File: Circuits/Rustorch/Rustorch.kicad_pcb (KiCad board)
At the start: 2 copper layers, 95 x 72 mm, 57 parts, among them CN1 USB_C_Receptacle_USB2.0_16P, CN2 OLED_128x64_IIC, Q1 2SC1815, Q2 2SC1815, Q3 2SC1815, Q4 2SC1815, SW1 SW_POWER (5P), SW2 RESET, SW3 SW_BOOT, SW4 SW_UP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

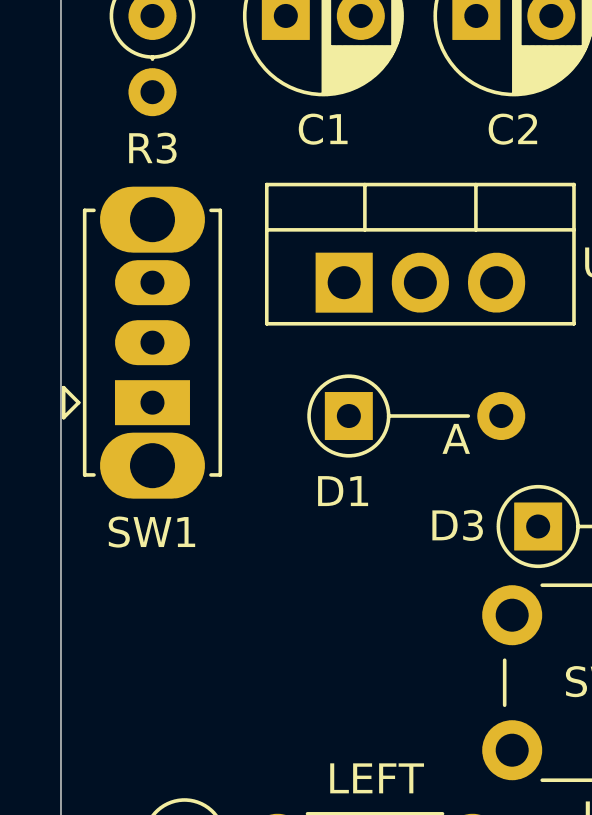
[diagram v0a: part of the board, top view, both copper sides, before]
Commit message: (Rustorch) 基板の電源スイッチを修正
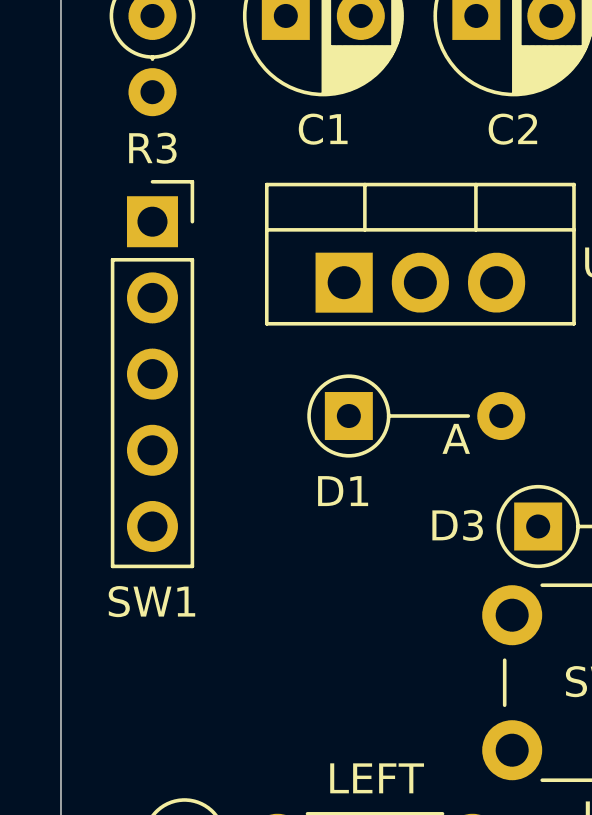
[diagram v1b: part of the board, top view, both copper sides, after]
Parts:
- SW1: value SW_POWER (5P) -> ToggleSW 3P; footprint Button_Switch_THT:SW_Slide_SPDT_Straight_CK_OS102011MS2Q -> Connector_PinSocket_2.54mm:PinSocket_1x05_P2.54mm_Vertical
- moved SW1 6.03 mm to (103.5, 97.0), turned to 0 degrees
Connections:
- SW1 pad 1: VBUS -> unconnected-(SW1-Pin_1-Pad1)
- SW1 pad 2: +5V -> unconnected-(SW1-Pin_2-Pad2)
- SW1 pad 3: unconnected-(SW1-C-Pad3) -> VBUS

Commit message: (Rustorch) 配線作業 (4層化)
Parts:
- moved R6 8.15 mm to (167.1, 109.7), turned to -90 degrees
- moved R1 7.62 mm to (113.5, 71.1), turned to -90 degrees
- moved R2 7.62 mm to (116.5, 71.1), turned to -90 degrees
- moved R5 3.05 mm to (164.0, 109.7)
- moved D2 2.55 mm to (103.5, 83.1), turned to -90 degrees
- moved C2 2.54 mm to (116.9, 90.1), turned to 180 degrees
- moved C3 2.50 mm to (116.9, 85.7), turned to 180 degrees
- moved R7 0.63 mm to (184.2, 97.1)
- turned BZ1 to 180 degrees
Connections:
- U3 pad 8: Net-(Q1-C) -> unconnected-(U3-CC-Pad8)
- U4 pad 8: Net-(Q2-C) -> unconnected-(U4-CC-Pad8)
- U5 pad 8: Net-(Q3-C) -> unconnected-(U5-CC-Pad8)
- U6 pad 8: Net-(Q4-C) -> unconnected-(U6-CC-Pad8)
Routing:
- net +3.3V: track 0.00 -> 111.0 mm, vias 0 -> 1
- net Net-(R11-Pad1): track 0.00 -> 89.9 mm
- net KEY_IN3_IO8: track 0.00 -> 78.3 mm
- net Net-(R10-Pad1): track 0.00 -> 77.3 mm
- net KEY_IN1_IO9_BOOT: track 0.00 -> 75.7 mm
- net /E: track 0.00 -> 72.4 mm, vias 0 -> 4
- net /DP: track 0.00 -> 67.5 mm, vias 0 -> 4
- net /D: track 0.00 -> 61.9 mm, vias 0 -> 4
- net /F: track 0.00 -> 60.2 mm, vias 0 -> 4
- net /C: track 0.00 -> 58.3 mm, vias 0 -> 4
- net 7SEG_DIGIT4: track 0.00 -> 57.8 mm
- net /G: track 0.00 -> 55.0 mm, vias 0 -> 4
- net /B: track 0.00 -> 53.3 mm, vias 0 -> 4
- net /A: track 0.00 -> 50.8 mm, vias 0 -> 4
- net 7SEG_DIGIT3: track 0.00 -> 44.0 mm
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- added copper zone on In1.Cu, net GND
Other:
- copper layers 2 -> 4

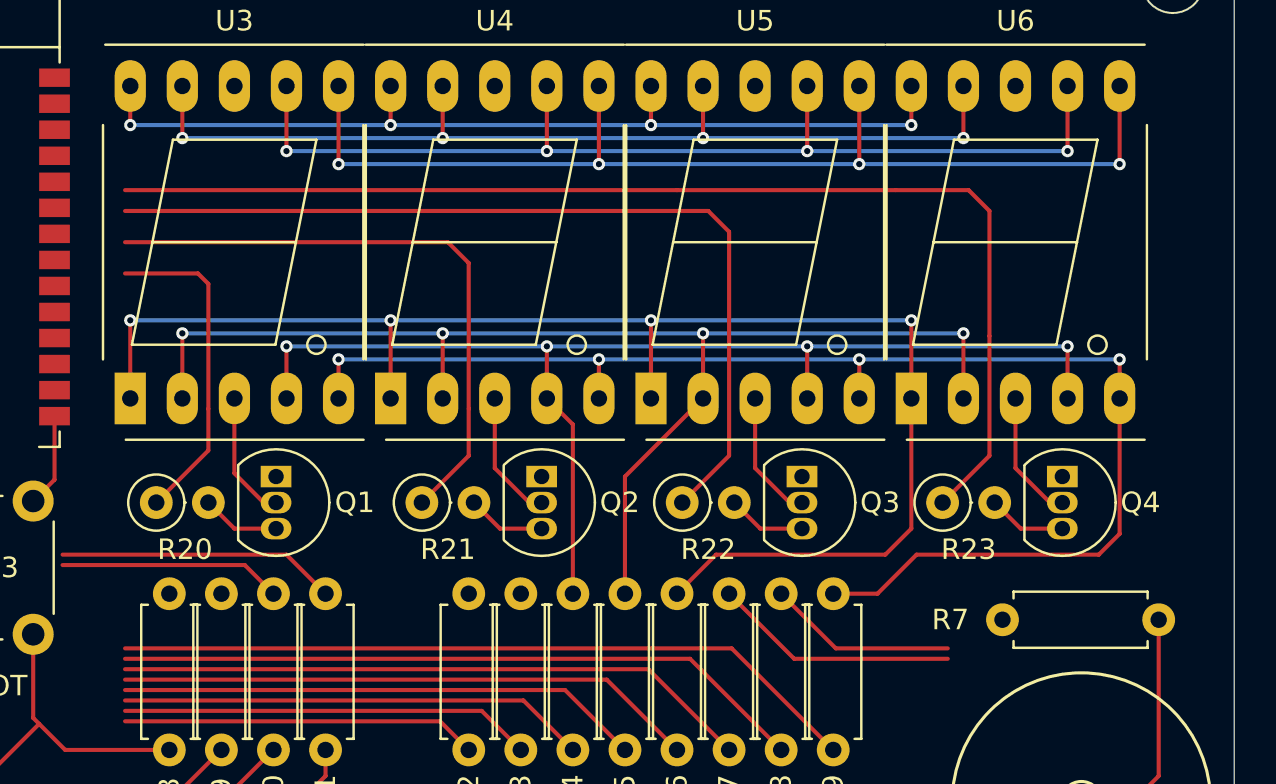
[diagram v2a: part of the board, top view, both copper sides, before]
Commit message: (Rustorch) 配線作業 (7セグ周辺)
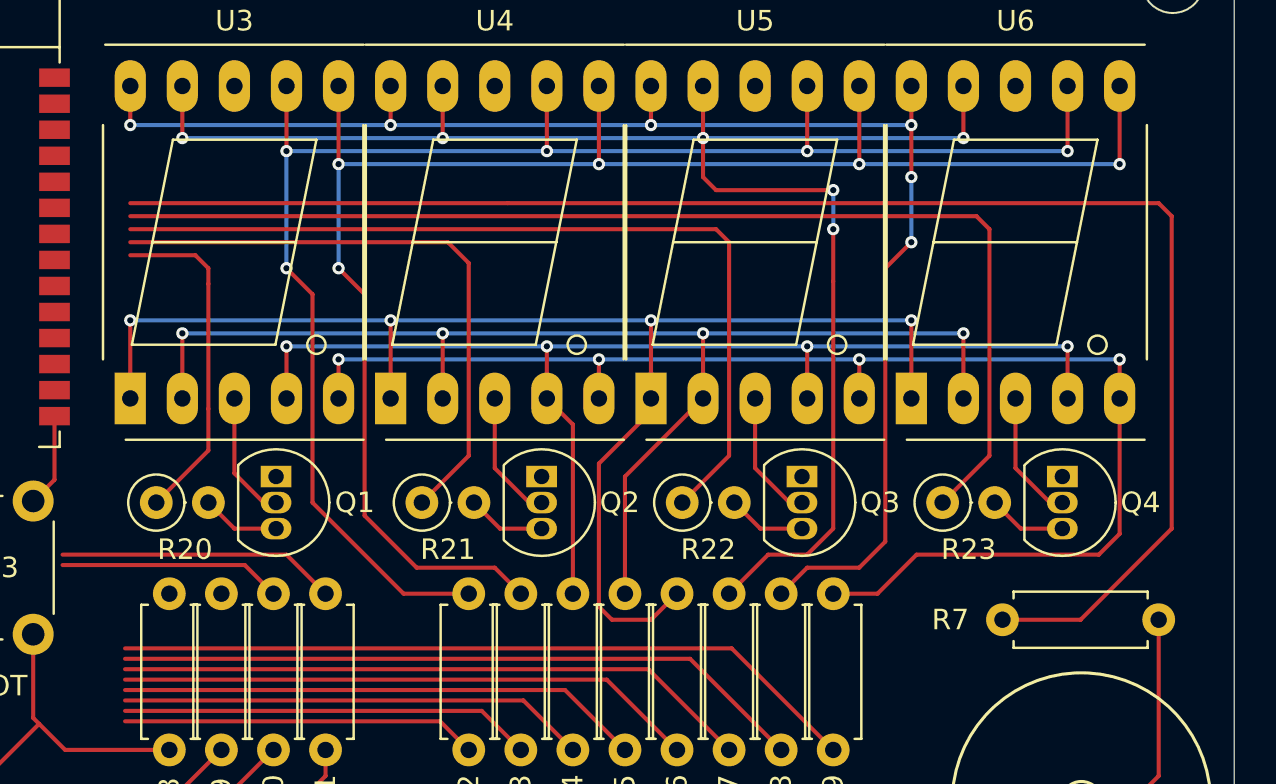
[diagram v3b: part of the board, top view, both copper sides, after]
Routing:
- net Net-(U1-MTMS/GPIO4/ADC1_CH4): track 0.00 -> 76.4 mm
- net /A: track 50.8 -> 77.9 mm, vias 4 -> 5
- net /B: track 53.3 -> 80.2 mm, vias 4 -> 5
- net /F: track 60.2 -> 79.7 mm, vias 4 -> 6
- net /G: track 55.0 -> 72.7 mm, vias 4 -> 6
- net Net-(D6-K): track 11.9 -> 18.4 mm
- net /E: track 72.4 -> 69.2 mm
- net 7SEG_DIGIT4: track 57.8 -> 56.5 mm
- net 7SEG_DIGIT3: track 44.0 -> 43.1 mm
- net 7SEG_DIGIT1: track 16.0 -> 16.6 mm

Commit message: (Rustorch) 配線作業 (一通り接続完了した状態)
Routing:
- net SDA: track 13.6 -> 74.8 mm, vias 0 -> 1
- net SCL: track 19.8 -> 77.9 mm, vias 0 -> 1
- net Net-(U1-MTDI/GPIO5/ADC1_CH5): track 25.5 -> 82.1 mm, vias 0 -> 3
- net KEY_IN2: track 20.3 -> 67.3 mm
- net KEY_IN3_IO8: track 78.3 -> 122.5 mm
- net 7SEG_E: track 28.3 -> 69.7 mm, vias 0 -> 2
- net 7SEG_D: track 25.6 -> 66.7 mm, vias 0 -> 2
- net 7SEG_A: track 17.5 -> 57.8 mm, vias 0 -> 2
- net 7SEG_B: track 20.1 -> 60.4 mm, vias 0 -> 2
- net 7SEG_C: track 22.8 -> 62.8 mm, vias 0 -> 2
- net KEY_OUT2: track 13.6 -> 50.0 mm, vias 0 -> 1
- net KEY_OUT1: track 10.9 -> 46.2 mm, vias 0 -> 1
- net 7SEG_G: track 33.8 -> 68.5 mm, vias 0 -> 2
- net 7SEG_DP: track 36.6 -> 70.9 mm
- net 7SEG_F: track 31.1 -> 65.3 mm, vias 0 -> 2
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- added copper zone on B.Cu, net GND
- added copper zone on F.Cu, net GND

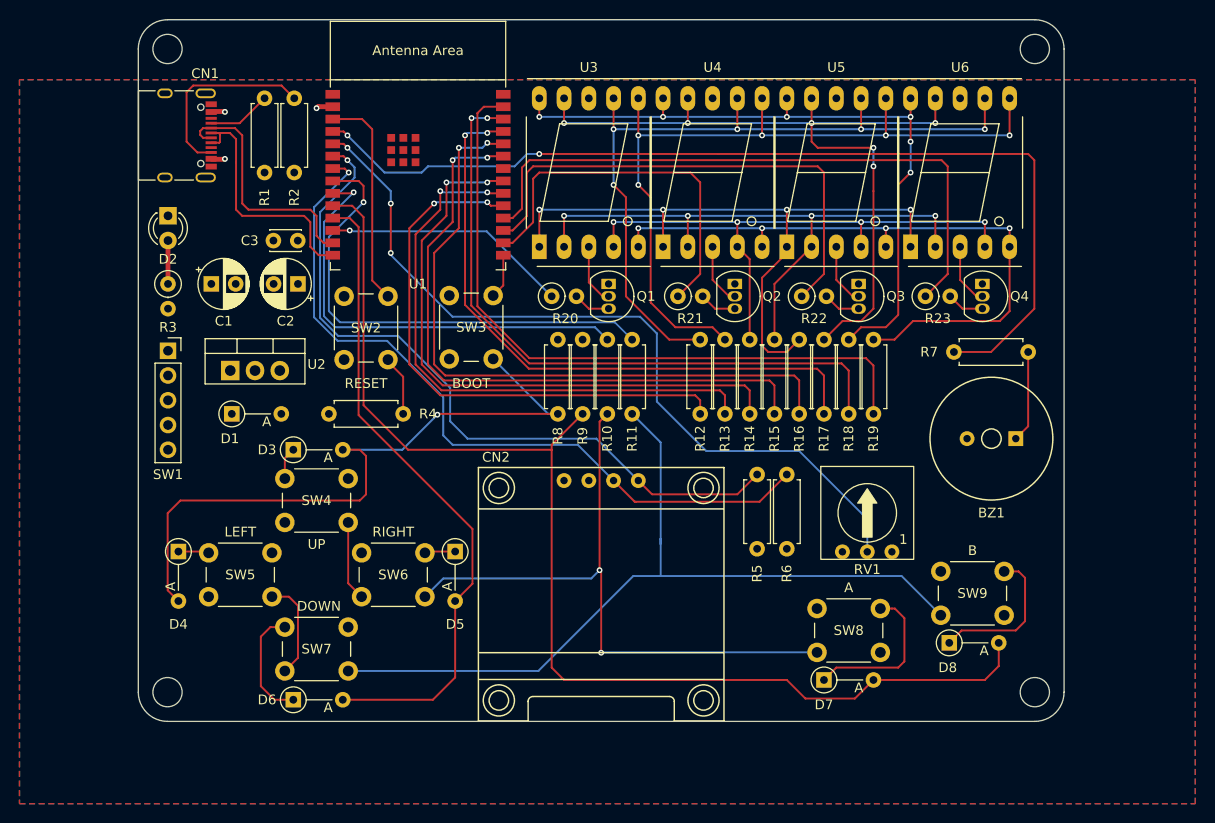
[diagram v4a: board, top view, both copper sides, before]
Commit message: (Rustorch) 配線作業 (表面に配線を集約中)
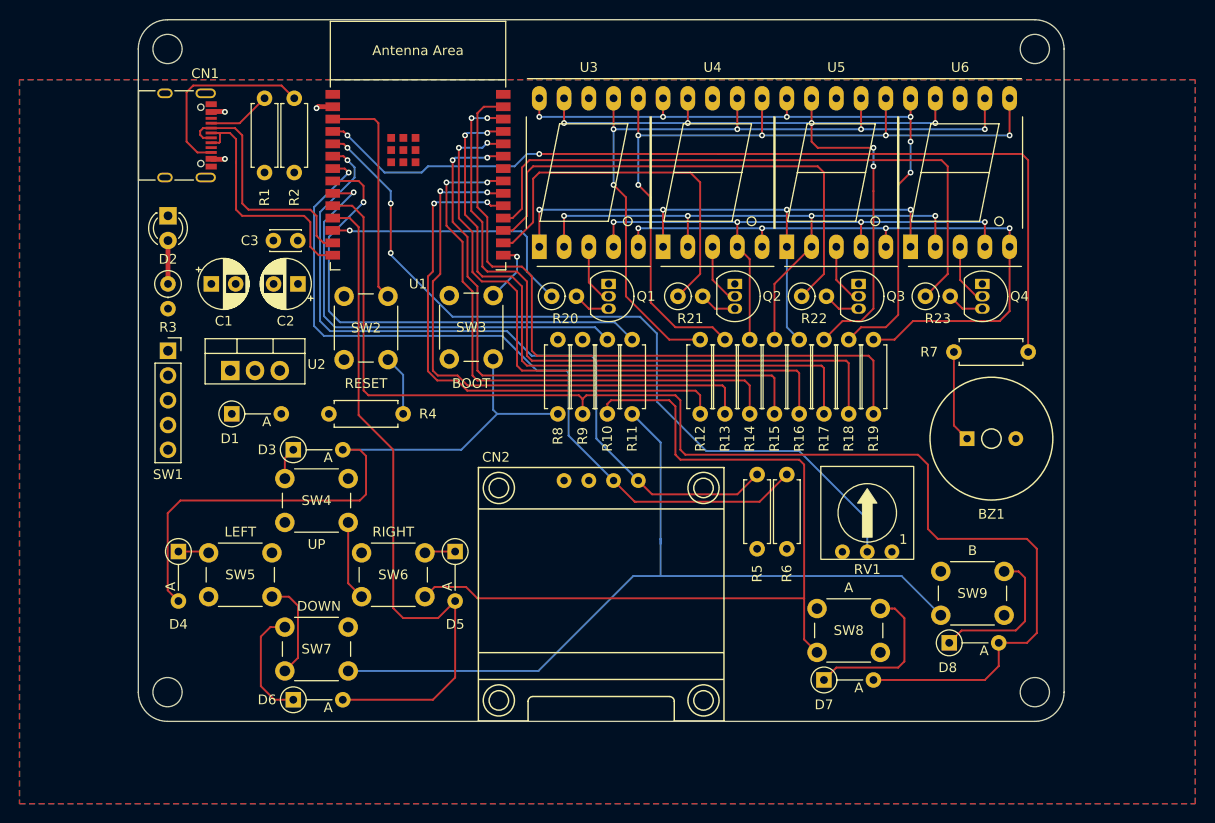
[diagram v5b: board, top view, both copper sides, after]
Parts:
- moved R7 7.62 mm to (191.8, 97.1), turned to 180 degrees
- turned BZ1 to 0 degrees
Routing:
- net Net-(R10-Pad1): track 93.8 -> 114.3 mm, vias 2 -> 0
- net KEY_IN3_IO8: track 122.5 -> 134.7 mm
- net Net-(U1-MTMS/GPIO4/ADC1_CH4): track 100.1 -> 93.8 mm
- net /E: track 69.2 -> 63.4 mm
- net 7SEG_E: track 69.7 -> 64.6 mm
- net 7SEG_D: track 66.7 -> 62.5 mm
- net 7SEG_C: track 62.8 -> 58.6 mm
- net KEY_IN2: track 67.3 -> 71.4 mm
- net SDA: track 74.8 -> 77.7 mm
- net 7SEG_F: track 65.3 -> 67.4 mm
- net 7SEG_DIGIT1: track 25.3 -> 27.3 mm
- net SCL: track 77.9 -> 80.0 mm
- net 7SEG_A: track 57.8 -> 55.8 mm
- net 7SEG_G: track 68.5 -> 70.4 mm
- net 7SEG_B: track 60.4 -> 58.7 mm
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
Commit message: (Rustorch) 配線作業 (MCU 裏の配線調整中)
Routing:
- net Net-(U1-MTDI/GPIO5/ADC1_CH5): track 82.1 -> 91.0 mm, vias 3 -> 1
- net KEY_OUT2: track 50.0 -> 44.6 mm
- net KEY_OUT1: track 46.2 -> 41.2 mm
- net Net-(U1-MTMS/GPIO4/ADC1_CH4): track 93.8 -> 97.7 mm
- net KEY_IN2: track 71.4 -> 74.5 mm
- net 7SEG_A: track 55.8 -> 56.9 mm
- net 7SEG_D: track 62.5 -> 63.5 mm
- net 7SEG_DIGIT1: track 27.3 -> 28.4 mm
- net KEY_IN1_IO9_BOOT: track 80.7 -> 81.8 mm
- net 7SEG_E: track 64.6 -> 65.6 mm
- net Net-(U1-EN/CHIP_PU): track 35.8 -> 34.8 mm, vias 0 -> 1
- net 7SEG_C: track 58.6 -> 59.4 mm
- net SDA: track 77.7 -> 78.5 mm
- net 7SEG_F: track 67.4 -> 68.2 mm
- net 7SEG_B: track 58.7 -> 59.2 mm

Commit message: (Rustorch) 配線作業 (MCU 周辺の裏面側配線を整理)
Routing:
- net KEY_IN2: track 74.5 -> 69.6 mm
- net Net-(R10-Pad1): track 114.3 -> 109.9 mm
- net 7SEG_DIGIT1: track 28.4 -> 32.5 mm
- net SDA: track 78.5 -> 74.9 mm
- net SCL: track 80.3 -> 78.2 mm
- net Net-(U1-MTDI/GPIO5/ADC1_CH5): track 91.0 -> 91.7 mm
- net Net-(U1-EN/CHIP_PU): track 34.8 -> 35.5 mm, vias 1 -> 2
- net Net-(R11-Pad1): track 114.7 -> 114.3 mm, vias 0 -> 1
- net KEY_IN1_IO9_BOOT: track 81.8 -> 81.5 mm, vias 1 -> 2
- net GND: vias 0 -> 1

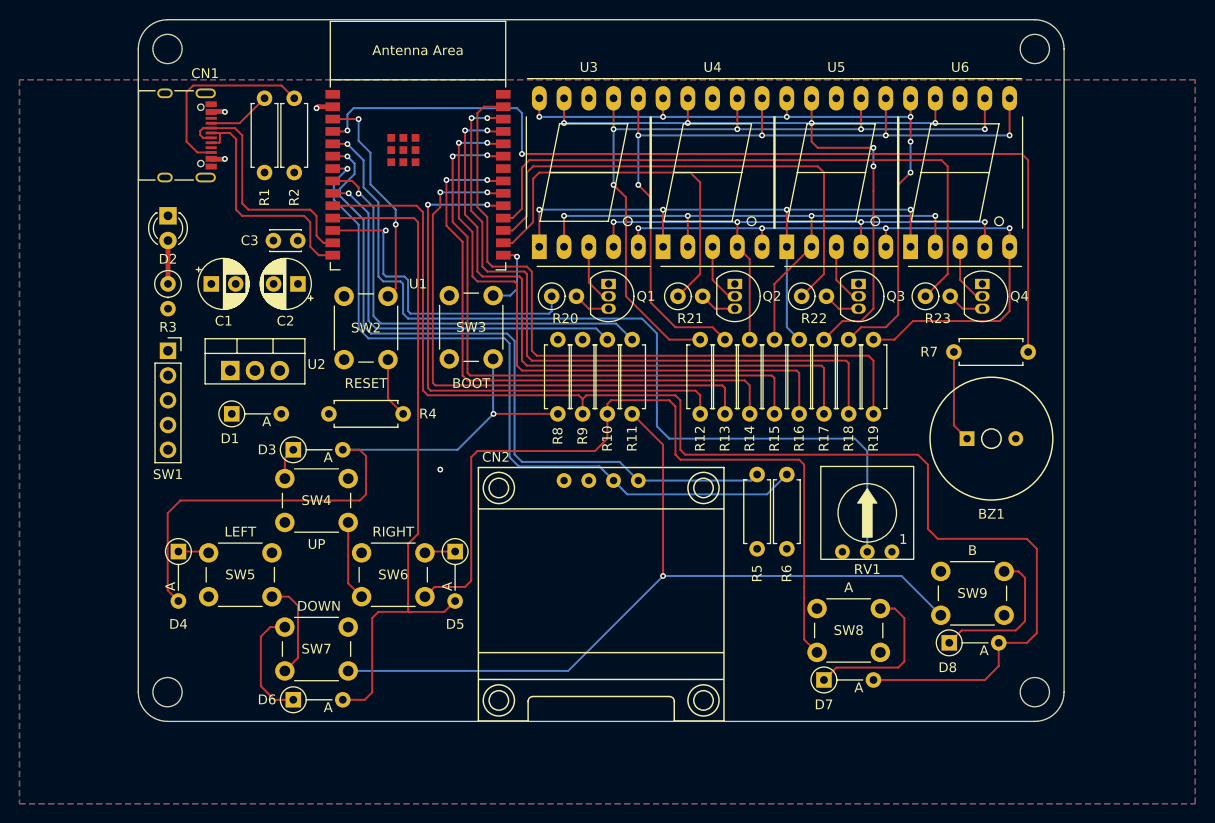
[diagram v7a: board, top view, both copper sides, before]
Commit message: (Rustorch) 配線作業 (4層から2層に削減するための準備)
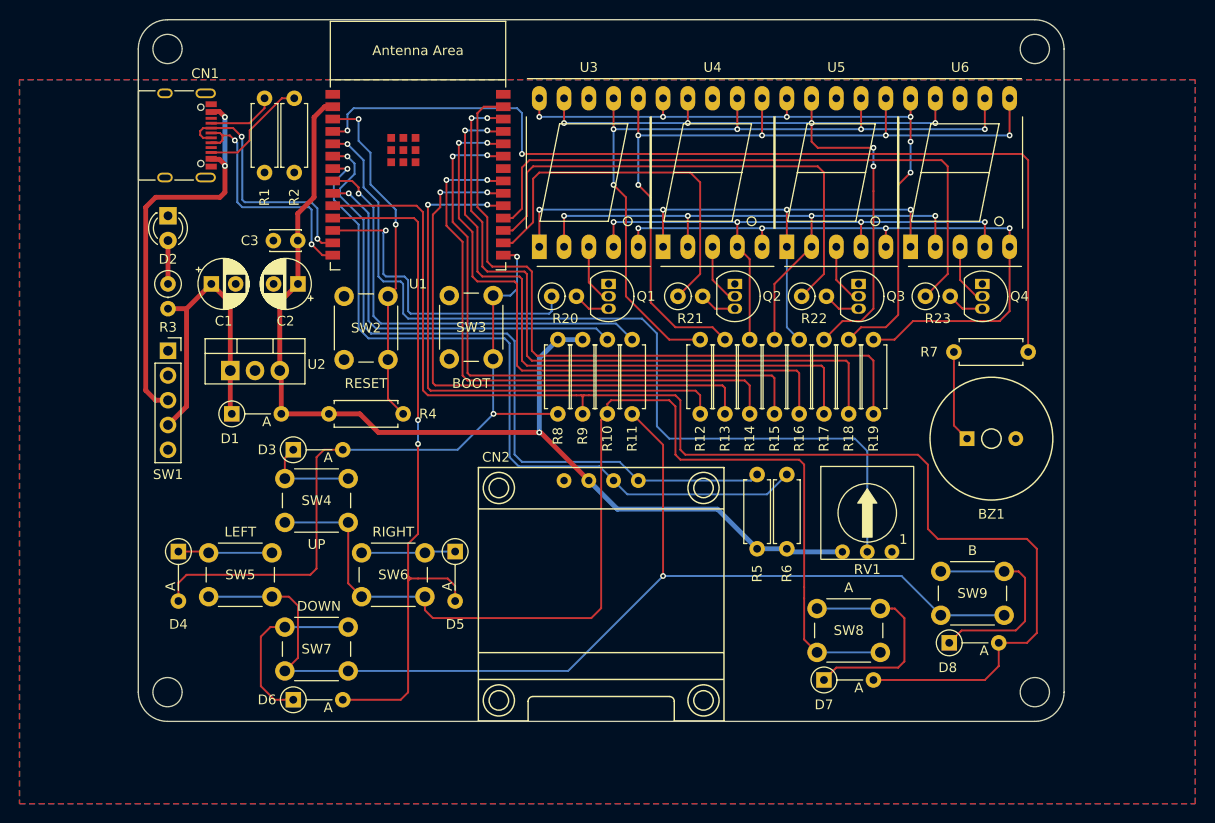
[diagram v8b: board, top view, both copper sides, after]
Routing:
- net Net-(CN1-CC2): track 19.9 -> 11.4 mm
- net KEY_IN1_IO9_BOOT: track 81.5 -> 75.4 mm
- net Net-(R10-Pad1): track 109.9 -> 115.0 mm
- net KEY_IN2: track 69.6 -> 72.0 mm, vias 0 -> 2
- net USB_D-: track 25.5 -> 27.9 mm, vias 0 -> 2
- net Net-(CN1-CC1): track 6.53 -> 7.13 mm
- net USB_D+: track 26.1 -> 26.5 mm, vias 0 -> 2
- net GND: vias 1 -> 0
- removed copper zone on In1.Cu, net GND
